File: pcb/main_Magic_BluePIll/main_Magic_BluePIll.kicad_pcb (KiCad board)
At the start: 2 copper layers, 95.3 x 113.2 mm, 50 parts, among them J2 MPU6050, J5 ESC, J9 Sensors, Q1 IRLML2502, SW1 Power_SW, SW2 PUSH_2, SW4 PUSH_1, U1 BluePill_SWD_Breakout, U2 AMS1117CD-3.3, U3 HC05, U6 CN3905

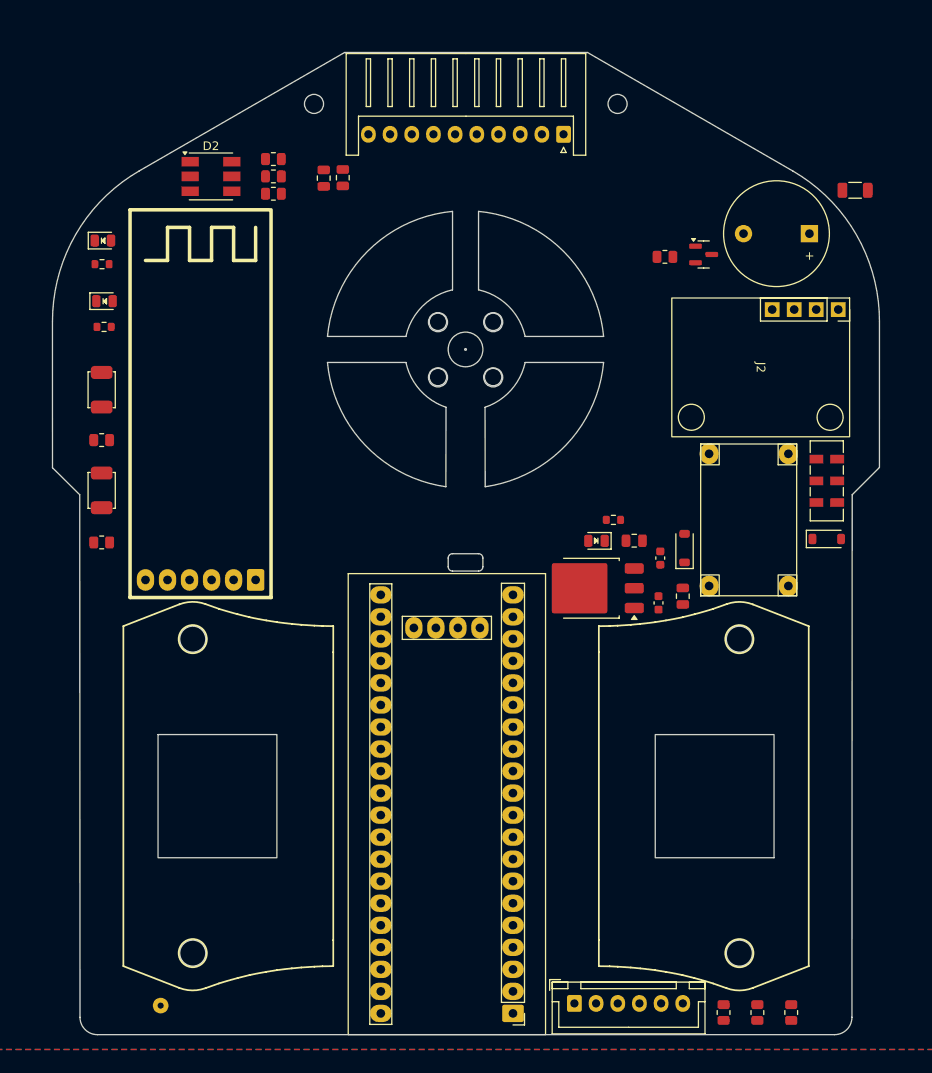
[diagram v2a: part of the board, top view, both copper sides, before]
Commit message: Routing of STM32F103 PCB done
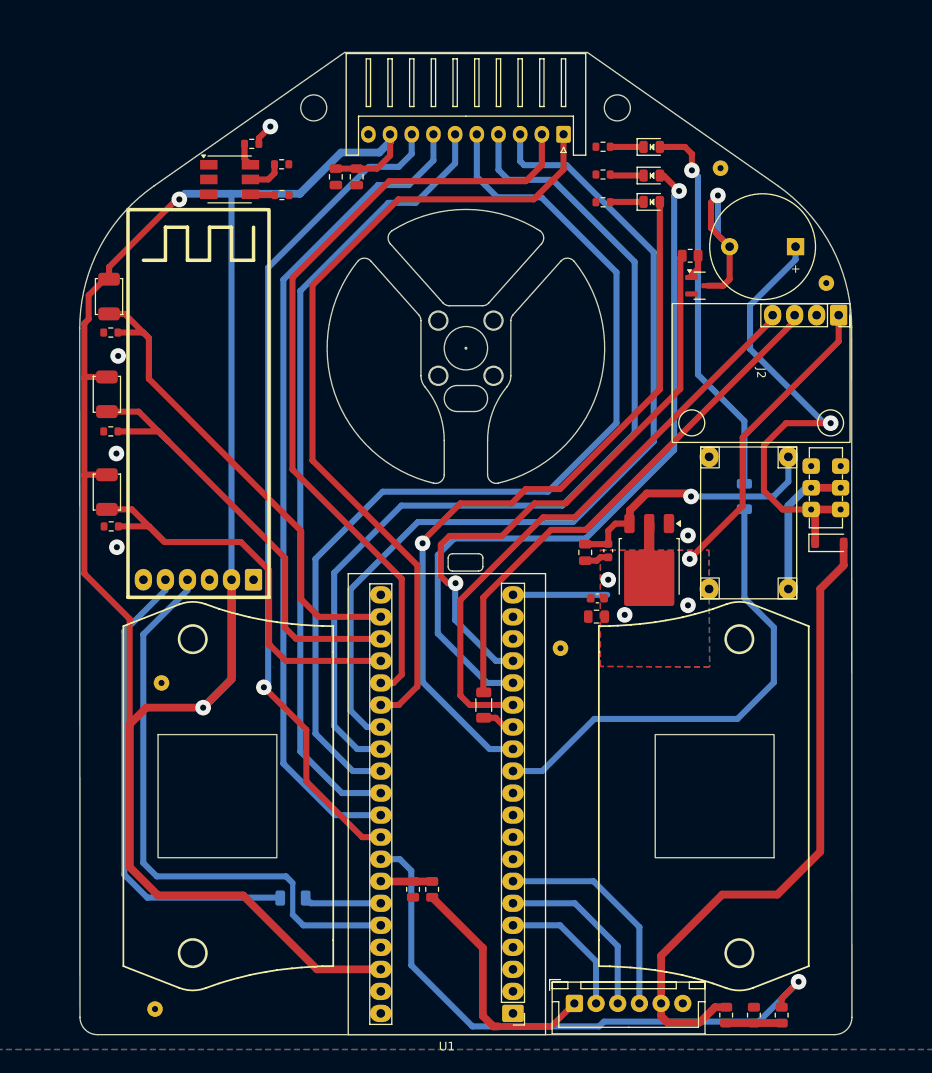
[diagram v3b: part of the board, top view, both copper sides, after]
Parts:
- removed the ? at (71.3, 234.7)
- removed D5: LED_3V3, MixLib:LED_0805_2012Metric
- added ?: , , F.Cu at (148.1, 151.3)
- added ?: , , F.Cu at (117.4, 193.4)
- added ?: , , F.Cu at (70.7, 235.1)
- added ?: , , F.Cu at (135.8, 138.1)
- added ?: , , F.Cu at (71.4, 197.4)
- added R14: 10k, Resistor_SMD:R_0805_2012Metric, F.Cu at (102.6, 221.2)
- added R16: 20k, Resistor_SMD:R_0805_2012Metric, F.Cu at (100.4, 221.2)
- added REF**: R_1206_3216Metric, Resistor_SMD:R_1206_3216Metric, F.Cu at (108.5, 200.0)
- added REF**: R_1206_3216Metric, Resistor_SMD:R_1206_3216Metric, B.Cu at (86.5, 222.2)
- added REF**: R_1206_3216Metric, Resistor_SMD:R_1206_3216Metric, B.Cu at (138.6, 175.9)
- added SW3: PUSH_3, MixLib:SW_Push_Sw-3424p_Handsolder, F.Cu at (65.3, 152.9)
- D3: value SS14 -> LED_BLUE; footprint Diode_SMD:D_SOD-123 -> MixLib:LED_0805_2012Metric
- D4: value LED_5V -> LED_BLUE
- H11, H12: value M2 -> M3; footprint MountingHole:MountingHole_2.2mm_M2 -> MountingHole:MountingHole_3mm
- R1, R9: footprint Resistor_SMD:R_0805_2012Metric -> Resistor_SMD:R_0603_1608Metric
- R10, R11, R12: value 470 -> 1k; footprint Resistor_SMD:R_0805_2012Metric -> Resistor_SMD:R_0603_1608Metric
- R13: value 4.7k -> 10k
- R2: value 100 -> 1k; footprint Resistor_SMD:R_1206_3216Metric -> Resistor_SMD:R_0603_1608Metric
- R7: value 4.7k -> 1k
- SW1: footprint Button_Switch_SMD:SW_DPDT_CK_JS202011JCQN -> MixLib:SW_DPDT_SLIDE_THT
- U1: footprint MixLib:BluePill_SWD -> MixLib:BluePill
- moved D6 65.5 mm to (127.8, 135.7)
- moved D4 63.7 mm to (127.8, 139.0)
- moved R13 61.8 mm to (65.5, 157.1)
- moved R6 61.2 mm to (122.3, 135.6), turned to 180 degrees
- moved R7 58.7 mm to (122.3, 138.8), turned to 180 degrees
- moved D3 40.1 mm to (127.8, 142.0), turned to 0 degrees
- moved R2 29.1 mm to (122.3, 142.0), turned to 180 degrees
- moved C7 10.2 mm to (121.5, 189.8), turned to 180 degrees
- moved U2 7.18 mm to (127.6, 184.1), turned to -90 degrees
- moved C5 7.07 mm to (121.7, 187.7), turned to 180 degrees
- moved C1 6.06 mm to (122.9, 182.2), turned to -90 degrees
- moved C6 5.81 mm to (120.2, 182.4), turned to -90 degrees
- moved C4 3.80 mm to (93.9, 139.1)
- moved Q1 3.63 mm to (133.4, 151.7)
- moved R12 3.05 mm to (81.8, 135.3)
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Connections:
- BZ1 pad 1: Net-(BZ1-+) -> /Vb
- D3 pad 1: +5V -> Net-(D3-K)
- D3 pad 2: Net-(D3-A) -> /LED_O
- D4 pad 2: +5V -> /LED_R
- D6 pad 2: /LED_BLUE -> /LED_G
- R13 pad 1: Net-(D5-K) -> GND
- R13 pad 2: GND -> /PUSH_3
- R2 pad 1: Net-(BZ1-+) -> Net-(D3-K)
- R2 pad 2: /Vb -> GND
- SW1 pad 1: Net-(U6-IN) -> /Vb
- SW1 pad 2: /Vb -> Net-(U6-IN)
- SW1 pad 4: Net-(U6-IN) -> /Vb
- SW1 pad 5: /Vb -> Net-(U6-IN)
- U1 pad 12: unconnected-(U1-PB4-Pad12) -> /LED_G
- U1 pad 13: unconnected-(U1-PB5-Pad13) -> /LED_O
- U1 pad 14: unconnected-(U1-PB6-Pad14) -> /SCL
- U1 pad 15: unconnected-(U1-PB7-Pad15) -> /SDA
- U1 pad 16: /SCL -> /LED_R
- U1 pad 17: /SDA -> /BUZ
- U1 pad 22: unconnected-(U1-PC13-Pad22) -> /PUSH_3
- U1 pad 23: unconnected-(U1-PC14-Pad23) -> /PUSH_2
- U1 pad 24: unconnected-(U1-PC15-Pad24) -> /PUSH_1
- U1 pad 25: unconnected-(U1-PA0-Pad25) -> /Data_1aux
- U1 pad 26: unconnected-(U1-PA1-Pad26) -> /Data_2aux
- U1 pad 27: unconnected-(U1-PA2-Pad27) -> /Data_SIG
- U1 pad 28: unconnected-(U1-PA3-Pad28) -> /Data_S3
- U1 pad 29: unconnected-(U1-PA4-Pad29) -> /Data_S2
- U1 pad 30: unconnected-(U1-PA5-Pad30) -> /Data_S1
- U1 pad 31: unconnected-(U1-PA6-Pad31) -> /Data_S0
- U1 pad 32: unconnected-(U1-PA7-Pad32) -> /Data_EN
- U1 pad 33: unconnected-(U1-PB0-Pad33) -> /V_bat
- U1 pad 34: unconnected-(U1-PB1-Pad34) -> /Curr_3V3
- U1 pad 35: unconnected-(U1-PB10-Pad35) -> /BL_RX
- U1 pad 36: unconnected-(U1-PB11-Pad36) -> /BL_TX
- U1 pad 5: unconnected-(U1-PA8-Pad5) -> /ESC_M3
- U1 pad 6: /BL_RX -> /ESC_M2
- U1 pad 7: /BL_TX -> /ESC_M1
- U6 pad 3: Net-(D3-A) -> +5V
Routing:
- net +3.3V: track 0.00 -> 299.1 mm, vias 0 -> 6
- net /Data_S2: track 0.00 -> 113.6 mm
- net /Data_S3: track 0.00 -> 109.4 mm
- net /Data_SIG: track 0.00 -> 104.9 mm
- net /LED_G: track 0.00 -> 100.3 mm, vias 0 -> 1
- net /Data_EN: track 0.00 -> 97.0 mm, vias 0 -> 1
- net /Data_S0: track 0.00 -> 95.5 mm
- net /Data_2aux: track 0.00 -> 94.9 mm
- net /Data_S1: track 0.00 -> 91.7 mm
- net /Data_1aux: track 0.00 -> 91.5 mm
- net /LED_O: track 0.00 -> 86.1 mm, vias 0 -> 1
- net /LED_R: track 0.00 -> 85.4 mm, vias 0 -> 1
- net /VM: track 0.00 -> 75.5 mm
- net /BUZ: track 0.00 -> 69.1 mm, vias 0 -> 1
- net /V_bat: track 0.00 -> 68.4 mm, vias 0 -> 1
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- added copper zone on B.Cu, net +3.3V
- added copper zone on F.Cu, net +3.3V
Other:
- board size 95.3 x 113.2 mm -> 89 x 113.2 mm
- board text removed: "Hacer el agarre de 3 puentes (no4). Agrandar turbina."

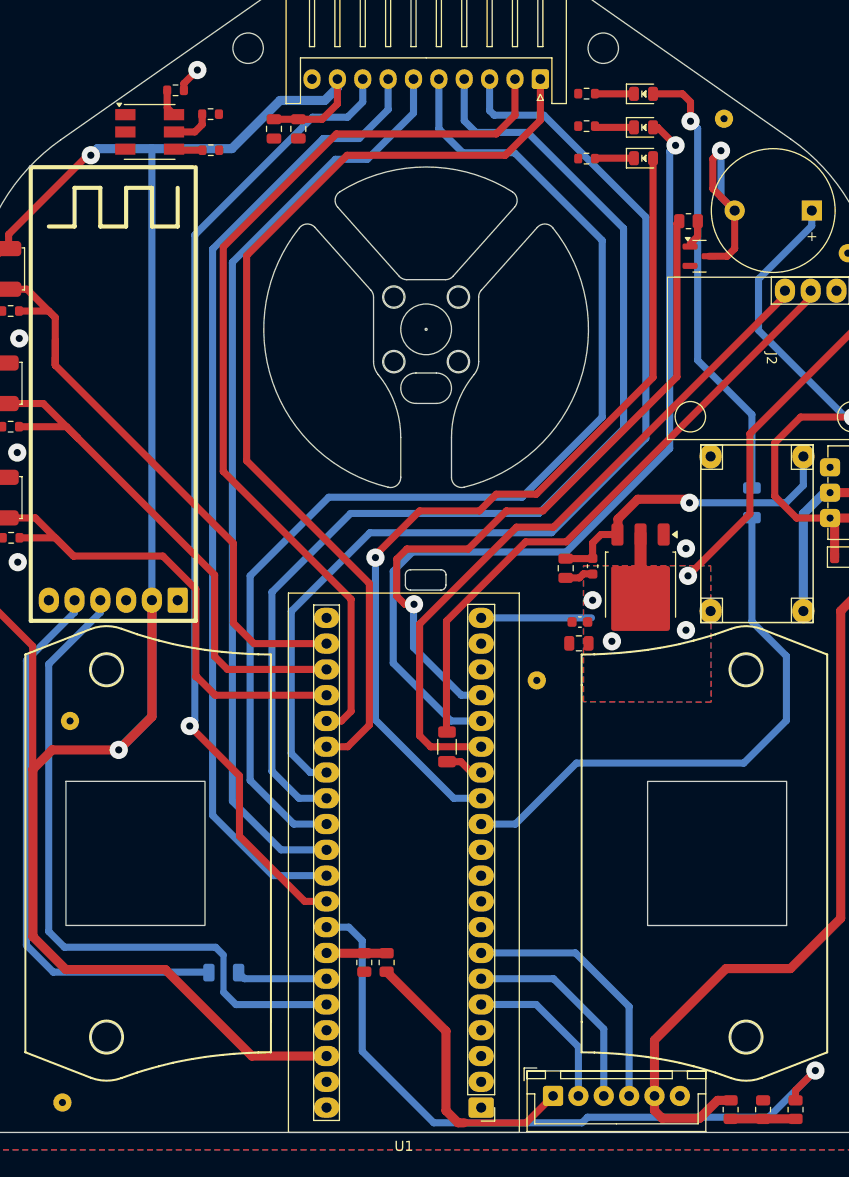
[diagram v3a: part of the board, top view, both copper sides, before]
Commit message: RGB led added to STM32 pcb
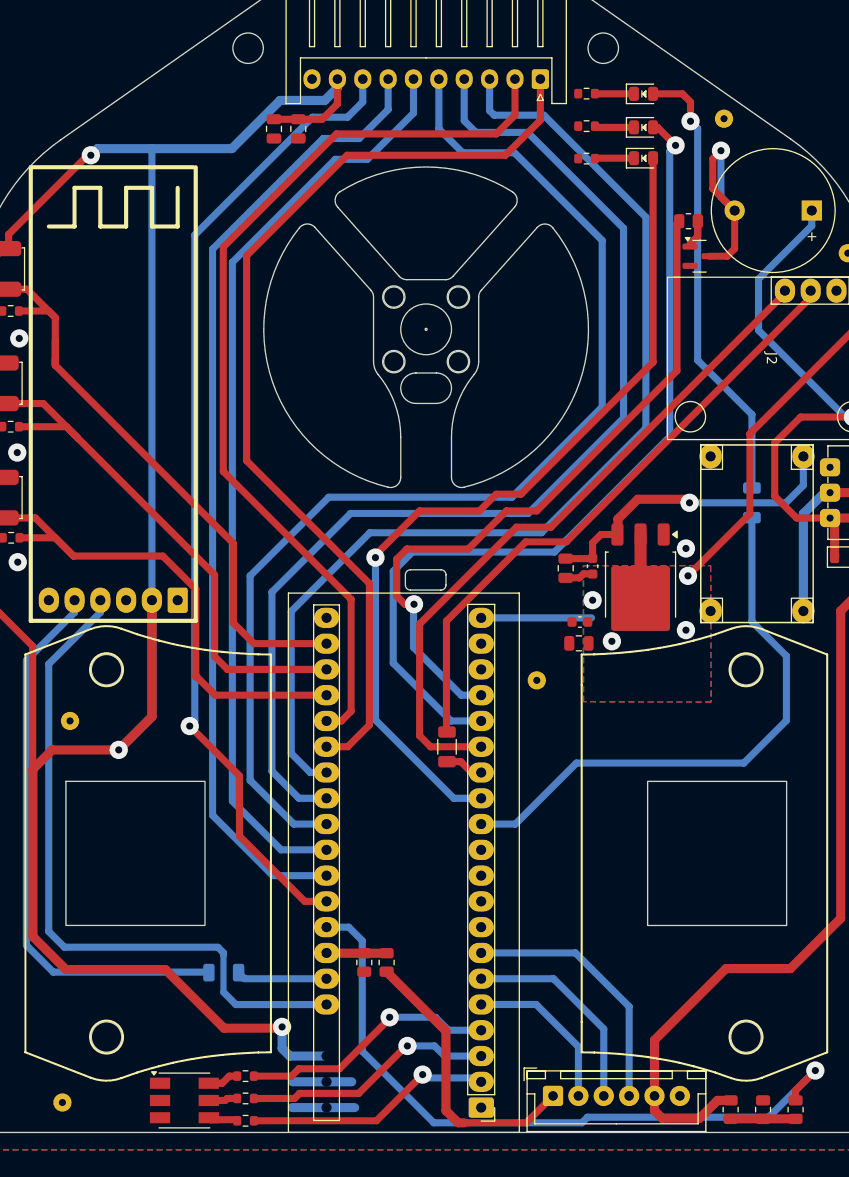
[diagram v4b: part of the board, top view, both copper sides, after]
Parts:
- moved R12 97.4 mm to (88.7, 232.4)
- moved R11 97.1 mm to (88.7, 234.7)
- moved R10 95.7 mm to (88.7, 236.8)
- moved D2 95.5 mm to (82.7, 234.8)
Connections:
- U1 pad 2: unconnected-(U1-PB13-Pad2) -> /RGB_B
- U1 pad 3: unconnected-(U1-PB14-Pad3) -> /RGB_G
- U1 pad 4: unconnected-(U1-PB15-Pad4) -> /RGB_R
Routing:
- net /RGB_G: track 0.00 -> 25.1 mm, vias 0 -> 1
- net /RGB_B: track 0.00 -> 24.6 mm, vias 0 -> 1
- net /RGB_R: track 2.55 -> 25.4 mm
- net GND: track 2.83 -> 14.8 mm
- net +3.3V: track 299.1 -> 300.4 mm, vias 6 -> 7
- net Net-(D2-GA): track 4.10 -> 2.88 mm
- net /LED_O: track 86.1 -> 85.2 mm
- net /LED_R: track 85.4 -> 84.7 mm
- net /Data_S3: track 109.4 -> 108.8 mm
- net /Data_SIG: track 104.9 -> 104.3 mm
- net /Data_S2: track 113.6 -> 113.0 mm
